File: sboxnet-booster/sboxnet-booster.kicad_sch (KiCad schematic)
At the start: 69 parts, among them J1 sboxnet-stecker_02x17, J2 cliff_FCR681465P_audiobuchse, J3 Conn_01x02_Male, J4 Conn_01x02_Male, J5 Screw_Terminal_01x04, J6 Screw_Terminal_01x04, J7 Conn_01x02_Male, U3 SN65HVD230, U4 l6206

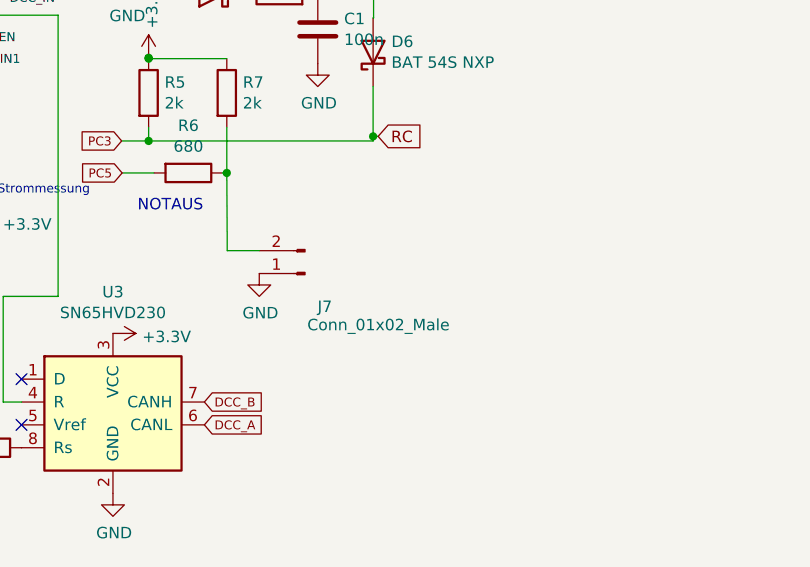
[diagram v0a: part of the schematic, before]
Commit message: correct l6206 footprint, notaus as terminal block
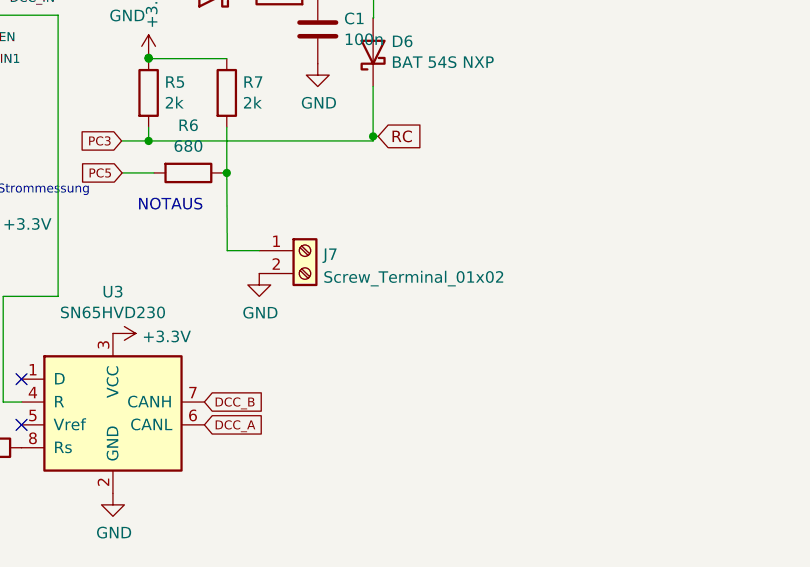
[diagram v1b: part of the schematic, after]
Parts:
- removed J7: Conn_01x02_Male, Connector_PinHeader_2.54mm:PinHeader_1x02_P2.54mm_Vertical, symbol Connector:Conn_01x02_Male
- added J7: Screw_Terminal_01x02, TerminalBlock:TerminalBlock_Altech_AK300-2_P5.00mm, symbol Connector:Screw_Terminal_01x02
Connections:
- net GND: now also J7.2 (Pin_2)
- net at R6.1, R7.2: now also J7.1 (Pin_1)
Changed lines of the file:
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@@
     (pin "1")
   )
-  (symbol (lib_id "Connector:Conn_01x02_Male") (at 84.328 128.016 180) (unit 1)
-    (in_bom yes) (on_board yes)
-    (property "Reference" "J7" (id 0) (at 85.725 131.699 0)
-      (effects (font (size 1.27 1.27)) (justify right))
-    )
-    (property "Value" "Conn_01x02_Male" (id 1) (at 84.582 133.731 0)
-      (effects (font (size 1.27 1.27)) (justify right))
-    )
-    (property "Footprint" "Connector_PinHeader_2.54mm:PinHeader_1x02_P2.54mm_Vertical" (id 2) (at 84.328 128.016 0)
+  (symbol (lib_id "Connector:Screw_Terminal_01x02") (at 84.328 125.476 0) (unit 1)
+    (in_bom yes) (on_board yes) (fields_autoplaced)
+    (property "Reference" "J7" (id 0) (at 86.36 125.9113 0)
+      (effects (font (size 1.27 1.27)) (justify left))
+    )
+    (property "Value" "Screw_Terminal_01x02" (id 1) (at 86.36 128.4482 0)
+      (effects (font (size 1.27 1.27)) (justify left))
+    )
+    (property "Footprint" "TerminalBlock:TerminalBlock_Altech_AK300-2_P5.00mm" (id 2) (at 84.328 125.476 0)
       (effects (font (size 1.27 1.27)) hide)
     )
-    (property "Datasheet" "~" (id 3) (at 84.328 128.016 0)
+    (property "Datasheet" "~" (id 3) (at 84.328 125.476 0)
       (effects (font (size 1.27 1.27)) hide)
     )
@@
       (reference "J6") (unit 1) (value "Screw_Terminal_01x04") (footprint "TerminalBlock:TerminalBlock_Altech_AK300-4_P5.00mm")
     )
-    (path "/df854d90-91a6-497c-aba1-6c00d8cc77a4"
-      (reference "J7") (unit 1) (value "Conn_01x02_Male") (footprint "Connector_PinHeader_2.54mm:PinHeader_1x02_P2.54mm_Vertical")
+    (path "/ec759541-1088-4e24-9c36-8a916e48ae55"
+      (reference "J7") (unit 1) (value "Screw_Terminal_01x02") (footprint "TerminalBlock:TerminalBlock_Altech_AK300-2_P5.00mm")
     )
     (path "/00000000-0000-0000-0000-000061b2babb"

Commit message: bat54s
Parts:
- D4, D5, D6: value BAT 54S NXP -> BAT 54S
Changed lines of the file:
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@@
     (in_bom yes) (on_board yes)
     (property "Reference" "D5" (id 0) (at 86.7664 80.2386 0))
-    (property "Value" "BAT 54S NXP" (id 1) (at 86.7664 82.55 0))
+    (property "Value" "BAT 54S" (id 1) (at 86.7664 82.55 0))
     (property "Footprint" "Package_TO_SOT_SMD:SOT-23_Handsoldering" (id 2) (at 86.7664 91.821 0)
       (effects (font (size 1.27 1.27)) hide)
@@
       (effects (font (size 1.27 1.27)) (justify right))
     )
-    (property "Value" "BAT 54S NXP" (id 1) (at 93.9292 104.5718 90)
+    (property "Value" "BAT 54S" (id 1) (at 93.9292 104.5718 90)
       (effects (font (size 1.27 1.27)) (justify right))
     )
@@
     (in_bom yes) (on_board yes)
     (property "Reference" "D4" (id 0) (at 73.8632 91.567 0))
-    (property "Value" "BAT 54S NXP" (id 1) (at 73.8632 93.8784 0))
+    (property "Value" "BAT 54S" (id 1) (at 73.8632 93.8784 0))
     (property "Footprint" "Package_TO_SOT_SMD:SOT-23_Handsoldering" (id 2) (at 73.8632 92.6338 0)
       (effects (font (size 1.27 1.27)) hide)
@@
     )
     (path "/00000000-0000-0000-0000-00005f1b960f"
-      (reference "D4") (unit 1) (value "BAT 54S NXP") (footprint "Package_TO_SOT_SMD:SOT-23_Handsoldering")
+      (reference "D4") (unit 1) (value "BAT 54S") (footprint "Package_TO_SOT_SMD:SOT-23_Handsoldering")
     )
     (path "/00000000-0000-0000-0000-00005f0e2174"
-      (reference "D5") (unit 1) (value "BAT 54S NXP") (footprint "Package_TO_SOT_SMD:SOT-23_Handsoldering")
+      (reference "D5") (unit 1) (value "BAT 54S") (footprint "Package_TO_SOT_SMD:SOT-23_Handsoldering")
     )
     (path "/00000000-0000-0000-0000-00005f139ee6"
-      (reference "D6") (unit 1) (value "BAT 54S NXP") (footprint "Package_TO_SOT_SMD:SOT-23_Handsoldering")
+      (reference "D6") (unit 1) (value "BAT 54S") (footprint "Package_TO_SOT_SMD:SOT-23_Handsoldering")
     )
     (path "/00000000-0000-0000-0000-00005dba95ff"

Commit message: cleanup
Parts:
- removed C10: 1u, Capacitor_SMD:C_1206_3216Metric, symbol Device:C
- removed J3, J4: Conn_01x02_Male, Connector_PinHeader_2.54mm:PinHeader_1x02_P2.54mm_Vertical, symbol Connector:Conn_01x02_Male
- removed R25: 0.22, Resistor_THT:R_Axial_DIN0614_L14.3mm_D5.7mm_P15.24mm_Horizontal, symbol Device:R
- removed R26, R28: 10k, Resistor_SMD:R_1206_3216Metric_Pad1.30x1.75mm_HandSolder, symbol Device:R
- removed U4: l6206, Package_DIP:DIP-24_W7.62mm_Socket, symbol sboxnet:l6206
- added C2: 1u, Capacitor_SMD:C_1206_3216Metric, symbol Device:C
- added J3, J4: Conn_01x03_Male, Connector_PinHeader_2.54mm:PinHeader_1x03_P2.54mm_Vertical, symbol Connector:Conn_01x03_Male
- added J8, J9: Conn_01x02_Male, Connector_PinHeader_2.54mm:PinHeader_1x02_P2.54mm_Vertical, symbol Connector:Conn_01x02_Male
- added R10, R13, R15: 10k, Resistor_SMD:R_1206_3216Metric_Pad1.30x1.75mm_HandSolder, symbol Device:R
- added R14: 0.22, Resistor_THT:R_Axial_DIN0614_L14.3mm_D5.7mm_P15.24mm_Horizontal, symbol Device:R
- added TP13, TP14, TP15: TestPoint, Connector_PinHeader_2.54mm:PinHeader_1x01_P2.54mm_Vertical, symbol Connector:TestPoint
- added U1: L6206PSO-sboxnet, sboxnet:HSOP-36-1EP_11.0x15.9mm_P0.65mm_SlugDown_ThermalVias, symbol sboxnet:L6206PSO-sboxnet
- C7: value 2700u/25v -> 2200u/25v; footprint Capacitor_THT:CP_Radial_D12.5mm_P5.00mm -> Capacitor_THT:CP_Axial_L30.0mm_D15.0mm_P35.00mm_Horizontal
- R1, R2, R23, R3: value 680 -> 470
- R19: value 2.1k -> 2k
- R20: value 33k -> 10k
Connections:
- net EN: now also U1.29 (ENb), U1.8 (ENa)
- net GND: now also R12.1, R27.2, C2.1, R10.2, R13.2, R14.1, U1.1 (GND), U1.18 (GND), U1.19 (GND), U1.36 (GND), U1.37 (PLANE); no longer R27.1
- net IN1: now also U1.10 (IN1a), U1.27 (IN2b)
- net IN2: now also U1.11 (IN2a), U1.26 (IN1b)
- net OUT1a: now also TP10.1, J3.3 (Pin_3), J8.1 (Pin_1), U1.15 (OUT1a); no longer D10.2 (A), D9.1 (K), J6.1 (Pin_1), J6.2 (Pin_2), J6.3 (Pin_3), J6.4 (Pin_4), R17.2, TP6.1
- net OUT1b: now also J3.1 (Pin_1), J8.2 (Pin_2), U1.22 (OUT1b)
- net OUT2a: now also J4.3 (Pin_3), J9.1 (Pin_1), TP13.1, U1.5 (OUT2a); no longer J5.1 (Pin_1), J5.2 (Pin_2), J5.3 (Pin_3), J5.4 (Pin_4), R16.1, R17.1, TP5.1
- net OUT2b: now also J4.1 (Pin_1), J9.2 (Pin_2), TP14.1, U1.32 (OUT2b); no longer TP10.1
- net PA0: now also C2.2, R15.1; no longer C9.2, R11.2
- net PA2: now also C9.2, R11.1; no longer R12.2
- net PC3: now also U1.13 (OCDa), U1.24 (OCDb)
- net V: now also R10.1, U1.33 (VSb), U1.4 (VSa)
- net at J1.21 (Pin_21), U3.4 (R): now also TP15.1
- net vboot: now reaches C11.2, D15.1 (K), TP8.1
- net vboot: now also U1.30 (VBOOT)
- net vcp: now reaches C12.1
- net vcp: now also U1.7 (VCP)
- new net: D10.2 (A), D9.1 (K), J3.2 (Pin_2), J6.1 (Pin_1), J6.2 (Pin_2), J6.3 (Pin_3), J6.4 (Pin_4), R17.2, TP6.1
- new net: J4.2 (Pin_2), J5.1 (Pin_1), J5.2 (Pin_2), J5.3 (Pin_3), J5.4 (Pin_4), R16.1, R17.1, TP5.1
- new net: R11.2, R14.2, U1.25 (SENSEb)
- new net: R13.1, U1.28 (PROGCLb)
- new net progcl_a: R12.2, U1.9 (PROGCLa)
- new net sensea: R15.2, R27.1, U1.12 (SENSEa)
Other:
- note added: "Bridge A"
- note added: "Bridge B"
- note added: "Parallel"
- note removed: "GND Pins für Wärmeableitung"
- note removed: "bl"
- moved on the sheet: C9, R11, R27, TP10, TP11, TP5

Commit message: sboxnet_booster smd v3
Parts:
- D12: value SK510/310 -> SK510
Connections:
- net IN1: now also U1.26 (IN1b); no longer U1.27 (IN2b)
- net IN2: now also U1.27 (IN2b); no longer U1.26 (IN1b)
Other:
- note added: "bridge select"
- note added: "parallel"
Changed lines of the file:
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@@
+    (effects (font (size 0.9906 0.9906)) (justify left bottom))
+  )
+  (text "bridge select" (at 145.796 60.452 0)
     (effects (font (size 0.9906 0.9906)) (justify left bottom))
   )
@@
   )
   (text "Bridge B" (at 154.686 80.518 0)
+    (effects (font (size 0.9906 0.9906)) (justify left bottom))
+  )
+  (text "parallel" (at 134.62 60.452 0)
     (effects (font (size 0.9906 0.9906)) (justify left bottom))
   )
@@
     (effects (font (size 0.9906 0.9906)) (justify left bottom))
   )
-  (label "in1_b" (at 200.406 121.92 0)
+  (label "in2_b" (at 200.406 121.92 0)
     (effects (font (size 0.9906 0.9906)) (justify left bottom))
   )
@@
     (effects (font (size 0.9906 0.9906)) (justify left bottom))
   )
-  (label "in2_b" (at 200.152 124.46 0)
+  (label "in1_b" (at 200.152 124.46 0)
     (effects (font (size 0.9906 0.9906)) (justify left bottom))
   )
@@
       (effects (font (size 1.27 1.27)) (justify right))
     )
-    (property "Value" "SK510/310" (id 1) (at 191.516 54.483 0)
+    (property "Value" "SK510" (id 1) (at 191.516 54.483 0)
       (effects (font (size 1.27 1.27)) (justify right))
     )
@@
     )
     (path "/00000000-0000-0000-0000-00005dba2ed7"
-      (reference "D12") (unit 1) (value "SK510/310") (footprint "Diode_SMD:D_SMB_Handsoldering")
+      (reference "D12") (unit 1) (value "SK510") (footprint "Diode_SMD:D_SMB_Handsoldering")
     )
     (path "/00000000-0000-0000-0000-00005f4c66f9"
